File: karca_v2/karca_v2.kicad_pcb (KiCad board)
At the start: 4 copper layers, 250 x 145 mm, 361 parts, among them J1 CON_FAN1, J10 Keyhole ignition switch, J11 Screw_Terminal_01x04, J12 Buzzer, J2 Conn_Batt, J3 USB_B_Micro, J4 LoadCell_1_2, J5 LoadCell_3_4, J6 Screw_Terminal_01x08, J7 Raspberry_pi, J8 Screw_Terminal_01x08, J9 Screw_Terminal_01x10, Q1 AO3401A, Q10 IRF3708, Q11 IRF3708, Q12 IRF3708, Q13 IRF3708, Q2 PN2222A, Q4 IRF3708, Q9 IRF3708, SW1 SW_SPST, SW2 SW_SPST, SW3 SW_SPST, U1 TVS1400DRV, U10 NUP4202, U11 M41T93, U12 NUP4202, U13 TLV9304xD, U14 TS5A3159ADBVR, U17 TS5A3159ADBVR, U19 TS5A3159ADBVR, U2 MCP3208, U22 TS5A3159ADBVR, U24 AD8495, U26 AD8495, U27 AD8495, U29 AD8495, U3 NUP4202, U30 INA180A4, U32 NUP4202, U33 AD8223, U34 INA180A2, U35 AD8223, U36 TLV9301xDBV, U4 TLV9304xD, U41 NUP4202, U42 MCP3204, U43 AD8223, U44 AD8223, U5 TLV9304xD, U6 TPS7A24, U7 TLV9304xD, U8 TLV9304xD, U9 MCP3208

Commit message: discrete traces
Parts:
- removed U16, U21: ~, Package_SON:VSON-8-1EP_3x3mm_P0.65mm_EP1.65x2.4mm_ThermalVias
- removed the U44 at (70.0, 135.5)
- added U27: AD8223, Package_SO:SOIC-8_3.9x4.9mm_P1.27mm, F.Cu at (69.6, 135.4)
- moved C10 58.3 mm to (229.7, 48.7)
- moved C11 58.3 mm to (231.2, 56.8)
- moved R6 58.3 mm to (233.2, 49.7)
- moved R7 58.3 mm to (233.4, 45.8)
- moved U6 58.3 mm to (232.9, 53.6)
- moved C31 54.6 mm to (76.7, 132.5), turned to 180 degrees
- moved C27 43.9 mm to (73.3, 114.3), turned to 180 degrees
- moved J5 40.2 mm to (36.3, 141.4), turned to 180 degrees
- moved J4 38.6 mm to (36.1, 97.4), turned to 180 degrees
- renumbered C3 to C10, C4 to C11, C64 to C12, C65 to C13, C5 to C14, C6 to C15, C53 to C16, C73 to C17, C7 to C18, C74 to C19, C72 to C2, C8 to C20, C9 to C21, C10 to C22, C75 to C23, C11 to C24, C12 to C25, C13 to C26, C76 to C27, C14 to C28, C15 to C29, C2 to C3, C16 to C30, C77 to C31, C17 to C32, C18 to C33, C19 to C34, C20 to C35, C21 to C36, C22 to C37, C23 to C38, C24 to C39, C66 to C4, C25 to C40, C26 to C41, C27 to C42, C28 to C43, C29 to C44, C30 to C45, C31 to C46, C32 to C47, C33 to C48, C34 to C49, C68 to C5, C35 to C50, C36 to C51, C37 to C52, C38 to C53, C39 to C54, C40 to C55, C41 to C56, C42 to C57, C43 to C58, C44 to C59, C67 to C6, C45 to C60, C46 to C61, C47 to C62, C48 to C63, C49 to C64, C50 to C65, C51 to C66, C52 to C67, C54 to C68, C55 to C69, C69 to C7, C56 to C70, C57 to C71, C58 to C72, C59 to C73, C60 to C74, C61 to C75, C70 to C76, C71 to C77, C62 to C8, C63 to C9, D22 to D21, D23 to D22, D24 to D23, F7 to F2, F2 to F3, F3 to F4, F4 to F5, F5 to F6, F6 to F7, Q4 to Q3, Q9 to Q4, Q10 to Q5, Q11 to Q6, Q12 to Q7, Q13 to Q8, R9 to R10, R96 to R100, R97 to R101, R98 to R102, R99 to R103, R100 to R104, R101 to R105, R102 to R106, R103 to R107, R104 to R108, R105 to R109, R106 to R110, R107 to R111, R108 to R112, R109 to R113, R110 to R114, R111 to R115, R112 to R116, R113 to R117, R114 to R118, R115 to R119, R116 to R62, R62 to R63, R63 to R64, R64 to R65, R65 to R66, R66 to R67, R117 to R68, R67 to R69, R68 to R70, R69 to R71, R70 to R72, R71 to R73, R118 to R74, R72 to R75, R73 to R76, R74 to R77, R75 to R78, R76 to R79, R10 to R8, R119 to R80, R77 to R81, R78 to R82, R79 to R83, R80 to R84, R81 to R85, R82 to R86, R83 to R87, R84 to R88, R85 to R89, R8 to R9, R86 to R90, R87 to R91, R88 to R92, R89 to R93, R90 to R94, R91 to R95, R92 to R96, R93 to R97, R94 to R98, R95 to R99, TP21 to TP20, TP20 to TP21, U12 to U10, U10 to U12, U33 to U15, U17 to U18, U35 to U19, U19 to U22, U43 to U23, U22 to U26, U24 to U30, U25 to U31, U37 to U32, U26 to U33, U38 to U34, U27 to U35, U28 to U36, U39 to U37, U29 to U38, U40 to U39, U30 to U40, U31 to U41, U32 to U42, U34 to U43, U42 to U44, U41 to U45, U36 to U46
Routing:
- net +12V: track 115.1 -> 320.8 mm, vias 2 -> 5
- net /DRV4_ADC: track 112.5 -> 168.3 mm
- net /Drivers/DRV5_ADC: track 189.0 -> 238.6 mm
- net /DRV3_ADC: track 101.9 -> 133.4 mm
- net /DRV2_ADC: track 114.6 -> 139.8 mm
- net /Drivers/IGN_CONT: track 256.4 -> 248.2 mm, vias 2 -> 1
- net +5V: track 101.4 -> 106.1 mm
- net /Drivers/IGN_POS: track 61.3 -> 58.7 mm
- net /Drivers/DRV1_CTL: track 202.9 -> 204.7 mm
- net Net-(U23-+RG): track 8.99 -> 9.83 mm

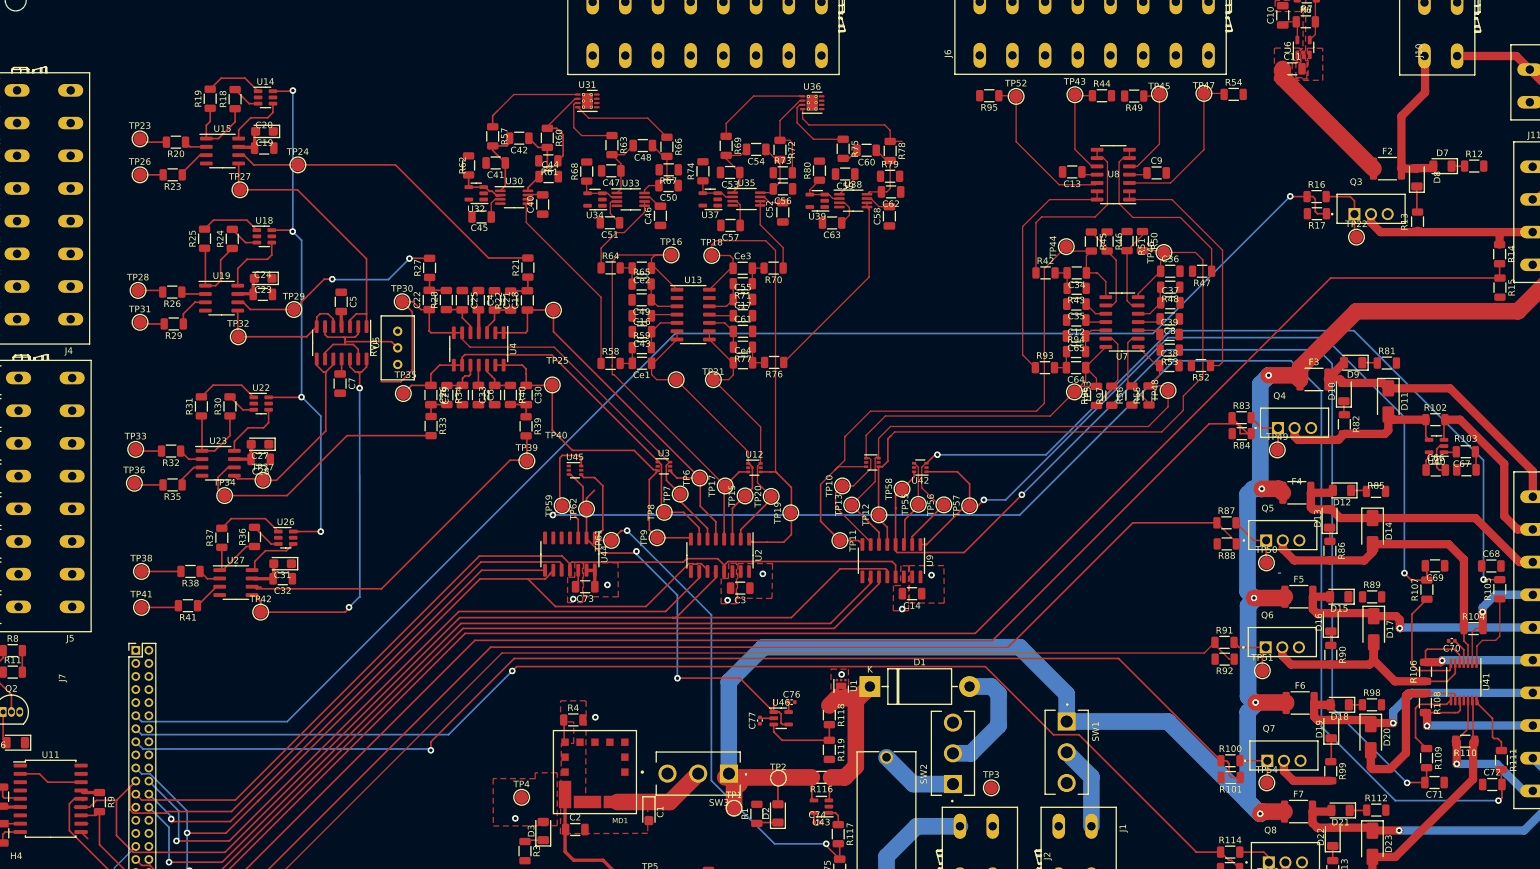
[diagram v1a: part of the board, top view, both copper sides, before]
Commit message: fixed TVS Diodes
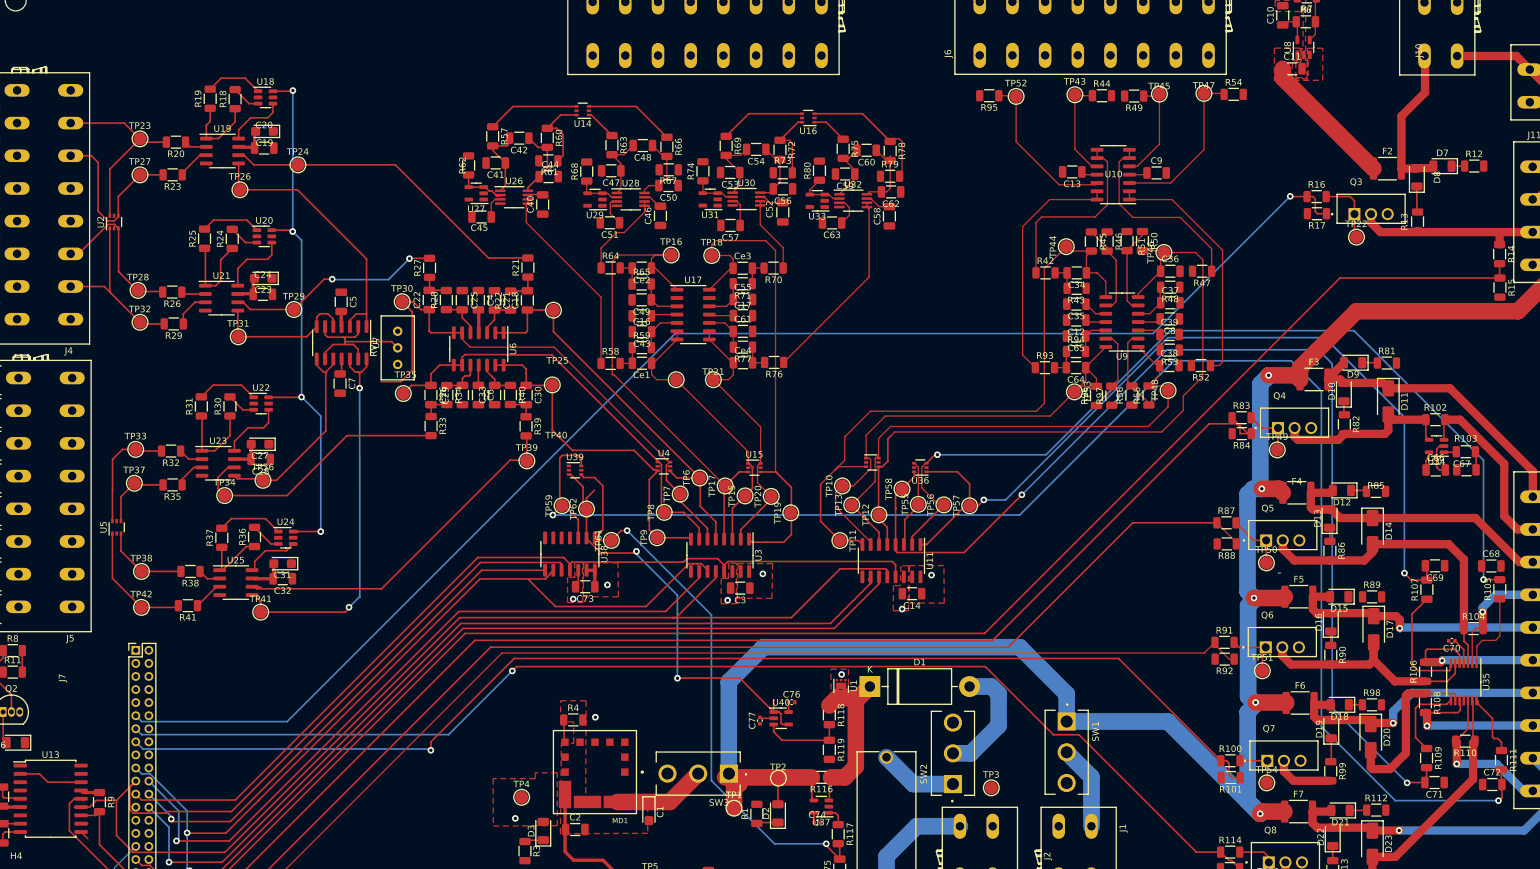
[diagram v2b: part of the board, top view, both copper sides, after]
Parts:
- removed the U31 at (123.3, 61.8)
- removed the U36 at (157.7, 62.0)
- added U14: NUP4202, Package_TO_SOT_SMD:SOT-363_SC-70-6, F.Cu at (122.6, 63.3)
- added U16: NUP4202, Package_TO_SOT_SMD:SOT-363_SC-70-6, F.Cu at (157.1, 64.4)
- added U2: NUP4202, Package_TO_SOT_SMD:SOT-363_SC-70-6, F.Cu at (50.9, 80.3)
- added U5: NUP4202, Package_TO_SOT_SMD:SOT-363_SC-70-6, F.Cu at (51.3, 127.0)
- renumbered TP27 to TP26, TP26 to TP27, TP32 to TP31, TP31 to TP32, TP37 to TP36, TP36 to TP37, TP42 to TP41, TP41 to TP42, U8 to U10, U9 to U11, U10 to U12, U11 to U13, U12 to U15, U13 to U17, U14 to U18, U15 to U19, U18 to U20, U19 to U21, U26 to U24, U27 to U25, U30 to U26, U32 to U27, U33 to U28, U34 to U29, U2 to U3, U35 to U30, U37 to U31, U38 to U32, U39 to U33, U40 to U34, U41 to U35, U42 to U36, U43 to U37, U44 to U38, U45 to U39, U3 to U4, U46 to U40, U4 to U6, U5 to U7, U6 to U8, U7 to U9
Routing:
- net /Load Cells/LC_Amplification/IN1: track 4.24 -> 29.5 mm
- net /Load Cells/LC_Amplification/IN2: track 3.54 -> 27.4 mm
- net /Load Cells/LC_Amplification1/IN2: track 3.80 -> 26.6 mm
- net /Load Cells/LC_Amplification1/IN1: track 3.88 -> 24.2 mm
- net /Load Cells/LC_Amplification2/IN1: track 4.05 -> 17.7 mm
- net /Load Cells/LC_Amplification3/IN2: track 5.76 -> 18.9 mm
- net /Load Cells/LC_Amplification3/IN1: track 6.04 -> 13.1 mm
- net /Load Cells/LC_Amplification2/IN2: track 4.48 -> 11.1 mm
- net /thermocouples/thermocouple_amp3/IN_1: track 11.6 -> 5.47 mm
- net /thermocouples/thermocouple_amp1/IN_1: track 10.6 -> 5.02 mm
- net /thermocouples/thermocouple_amp2/IN_2: track 14.4 -> 11.1 mm
- net Net-(U32--IN): track 6.70 -> 9.83 mm
- net /thermocouples/thermocouple_amp2/IN_1: track 15.4 -> 13.0 mm
- net /thermocouples/thermocouple_amp/IN_1: track 16.1 -> 14.1 mm
- net /thermocouples/thermocouple_amp3/IN_2: track 20.0 -> 21.8 mm
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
